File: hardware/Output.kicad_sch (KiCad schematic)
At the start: 26 parts, among them J10 Conn_Coaxial, J11 Conn_Coaxial, J12 Conn_Coaxial, J13 Conn_Coaxial, J14 Conn_Coaxial, J15 Conn_Coaxial, J8 Conn_Coaxial, J9 Conn_Coaxial, U29 74LVCH2T45DC, U30 74LVCH2T45DC

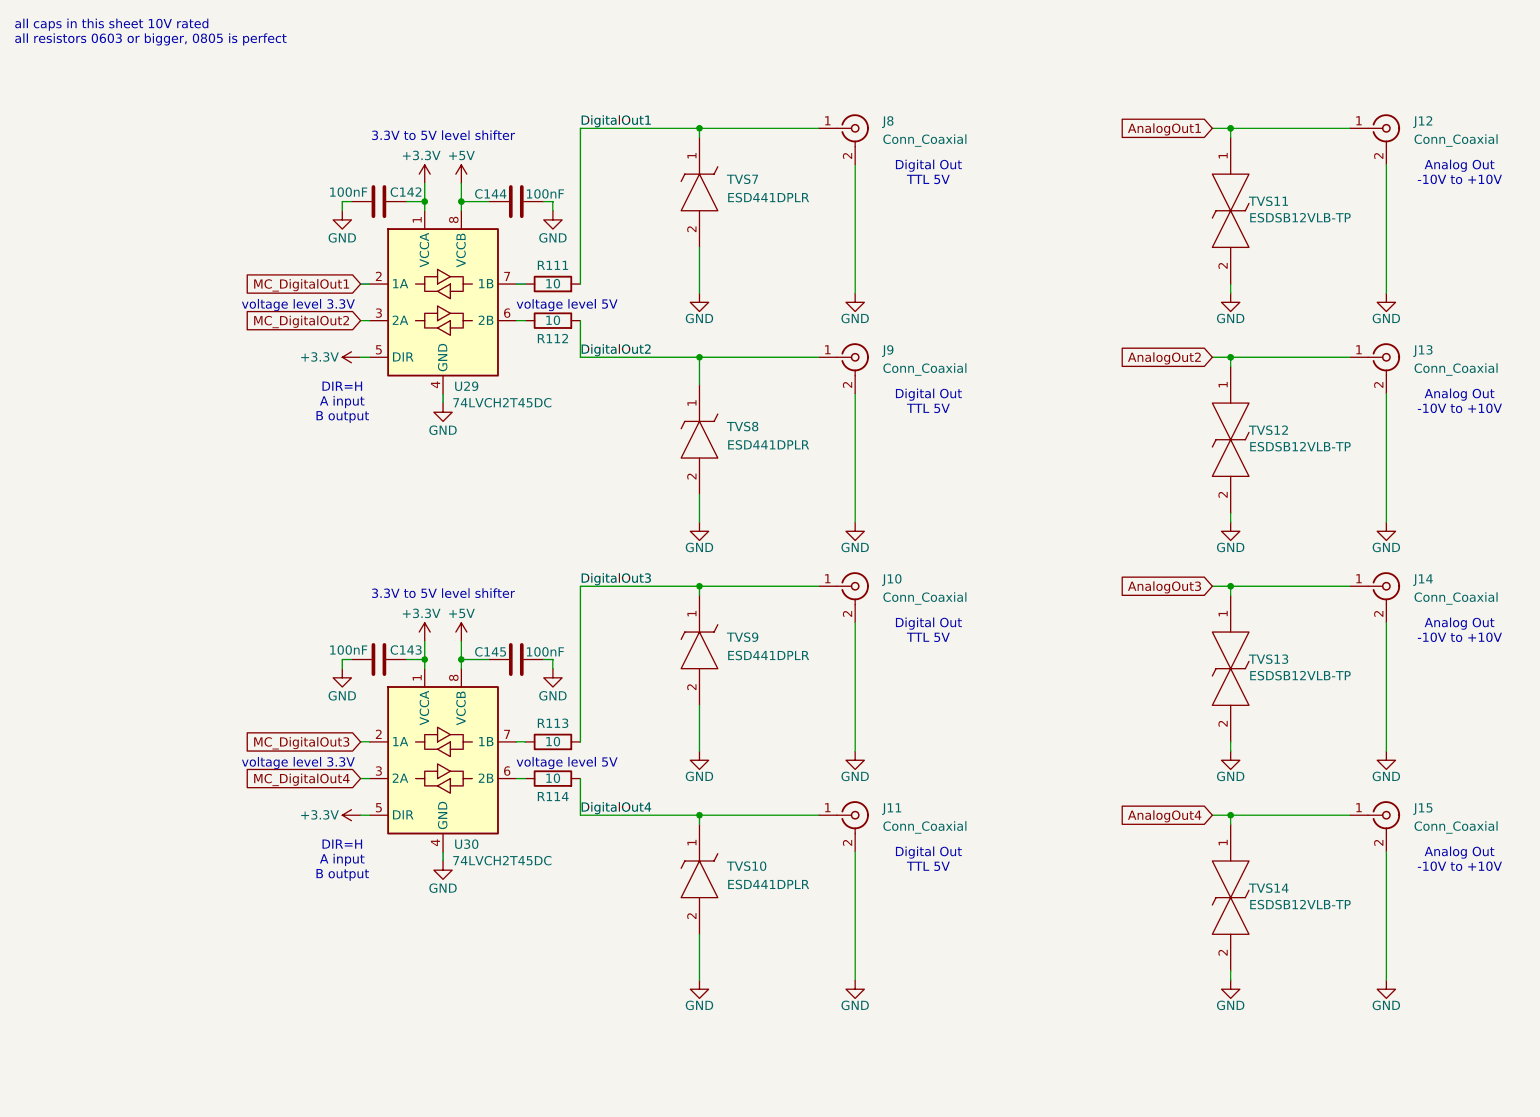
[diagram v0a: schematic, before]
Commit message: Added caps voltage rating + block diagram
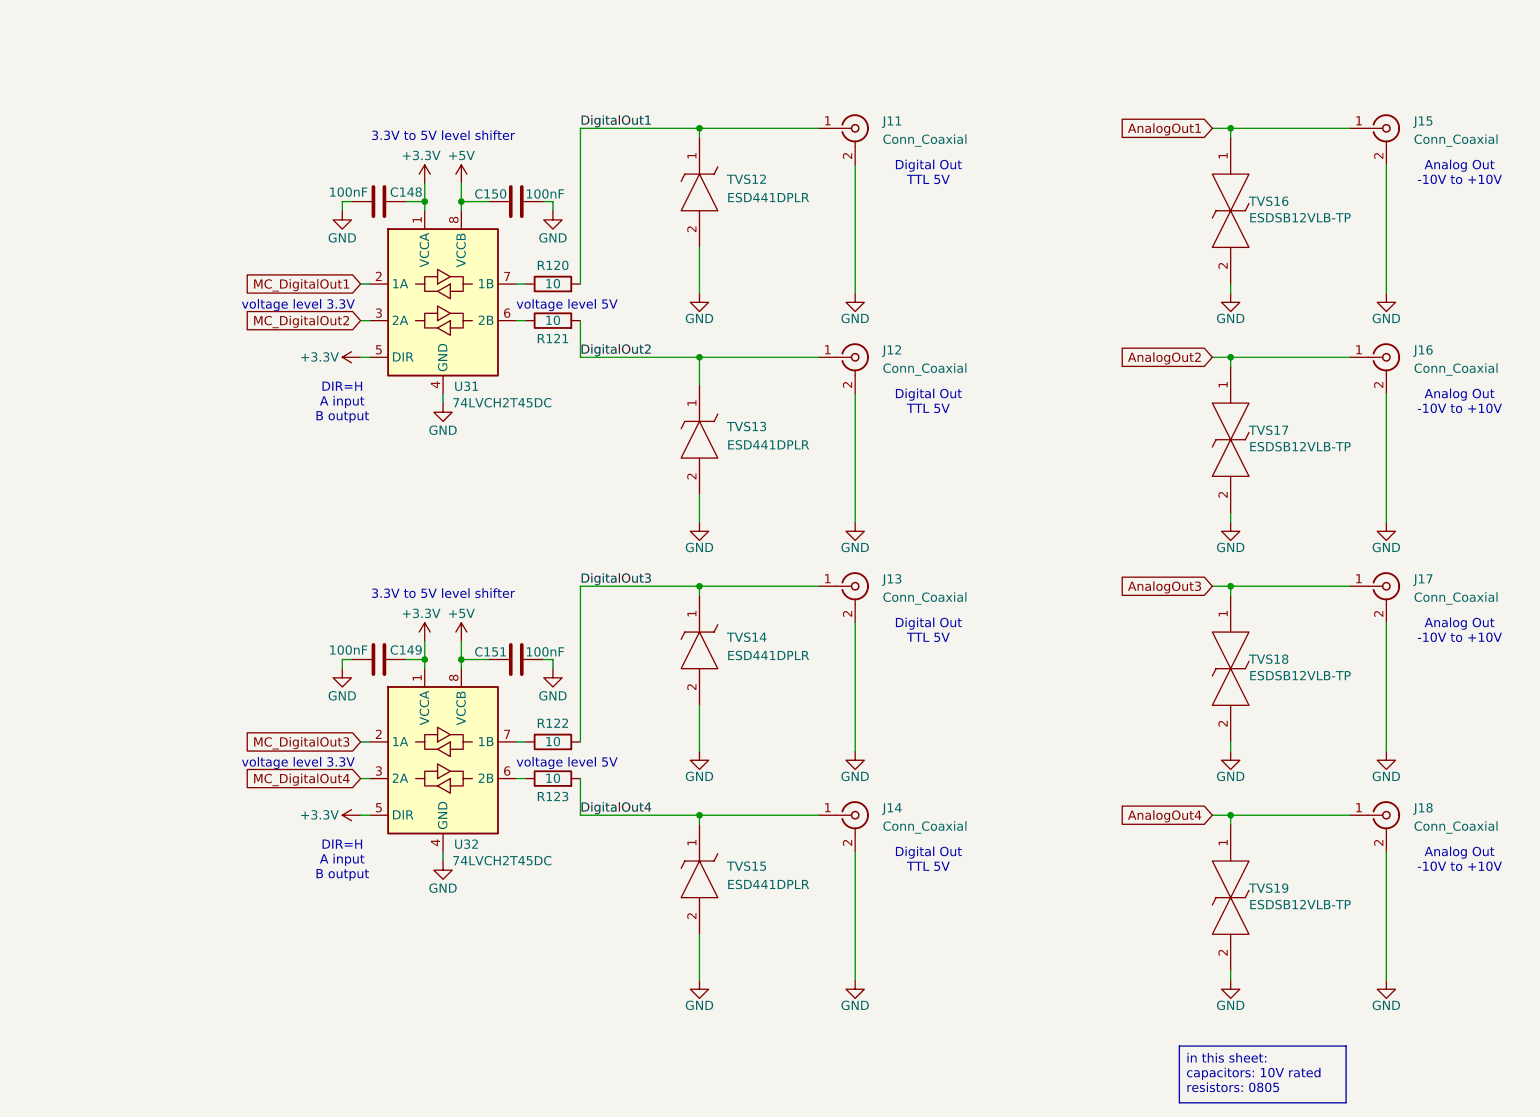
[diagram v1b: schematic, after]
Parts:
- renumbered C142 to C148, C143 to C149, C144 to C150, C145 to C151, J8 to J11, J9 to J12, J10 to J13, J11 to J14, J12 to J15, J13 to J16, J14 to J17, J15 to J18, R111 to R120, R112 to R121, R113 to R122, R114 to R123, TVS7 to TVS12, TVS8 to TVS13, TVS9 to TVS14, TVS10 to TVS15, TVS11 to TVS16, TVS12 to TVS17, TVS13 to TVS18, TVS14 to TVS19, U29 to U31, U30 to U32
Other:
- note removed: "all caps in this sheet 10V rated all resistors 0603 or bigger, 0805 is perfect"
- title: Multi Channel HARP DAC -> harp device quad dac

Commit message: The footprint assigning and reviewing have started.
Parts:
- C148, C149, C150, C151: symbol Device:C -> harp.device.quad.dac:C
- J11, J12, J13, J14, J15, J16, J17, J18: symbol Connector:Conn_Coaxial -> harp.device.quad.dac:Conn_Coaxial
- R120, R121, R122, R123: symbol Device:R -> harp.device.quad.dac:R
- TVS12, TVS13, TVS14, TVS15: symbol ESD441DPLR:ESD441DPLR -> harp.device.quad.dac:ESD441DPLR
- TVS16, TVS17, TVS18, TVS19: symbol ESDSB12VLB-TP:ESDSB12VLB-TP -> harp.device.quad.dac:ESDSB12VLB-TP
- U31, U32: symbol Logic_LevelTranslator:74LVCH2T45DC -> harp.device.quad.dac:74LVCH2T45DC
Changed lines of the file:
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@@
 	)
 	(symbol
-		(lib_id "Device:R")
+		(lib_id "harp.device.quad.dac:R")
 		(at 90.17 120.65 90)
 		(unit 1)
@@
 	)
 	(symbol
-		(lib_id "Connector:Conn_Coaxial")
+		(lib_id "harp.device.quad.dac:Conn_Coaxial")
 		(at 132.08 125.73 0)
 		(unit 1)
@@
 	)
 	(symbol
-		(lib_id "ESD441DPLR:ESD441DPLR")
+		(lib_id "harp.device.quad.dac:ESD441DPLR")
 		(at 110.49 95.25 270)
 		(unit 1)
@@
 	)
 	(symbol
-		(lib_id "Connector:Conn_Coaxial")
+		(lib_id "harp.device.quad.dac:Conn_Coaxial")
 		(at 205.74 62.23 0)
 		(unit 1)
@@
 	)
 	(symbol
-		(lib_id "Connector:Conn_Coaxial")
+		(lib_id "harp.device.quad.dac:Conn_Coaxial")
 		(at 205.74 125.73 0)
 		(unit 1)
@@
 	)
 	(symbol
-		(lib_id "Connector:Conn_Coaxial")
+		(lib_id "harp.device.quad.dac:Conn_Coaxial")
 		(at 132.08 62.23 0)
 		(unit 1)
@@
 	)
 	(symbol
-		(lib_id "Connector:Conn_Coaxial")
+		(lib_id "harp.device.quad.dac:Conn_Coaxial")
 		(at 132.08 93.98 0)
 		(unit 1)
@@
 	)
 	(symbol
-		(lib_id "Connector:Conn_Coaxial")
+		(lib_id "harp.device.quad.dac:Conn_Coaxial")
 		(at 205.74 93.98 0)
 		(unit 1)
@@
 	)
 	(symbol
-		(lib_id "ESD441DPLR:ESD441DPLR")
+		(lib_id "harp.device.quad.dac:ESD441DPLR")
 		(at 110.49 31.75 270)
 		(unit 1)
@@
 	)
 	(symbol
-		(lib_id "Device:C")
+		(lib_id "harp.device.quad.dac:C")
 		(at 85.09 40.64 270)
 		(unit 1)
@@
 	)
 	(symbol
-		(lib_id "Connector:Conn_Coaxial")
+		(lib_id "harp.device.quad.dac:Conn_Coaxial")
 		(at 132.08 30.48 0)
 		(unit 1)
@@
 	)
 	(symbol
-		(lib_id "Logic_LevelTranslator:74LVCH2T45DC")
+		(lib_id "harp.device.quad.dac:74LVCH2T45DC")
 		(at 74.93 118.11 0)
 		(unit 1)
@@
 	)
 	(symbol
-		(lib_id "Device:C")
+		(lib_id "harp.device.quad.dac:C")
 		(at 66.04 40.64 270)
 		(unit 1)
@@
 	)
 	(symbol
-		(lib_id "Logic_LevelTranslator:74LVCH2T45DC")
+		(lib_id "harp.device.quad.dac:74LVCH2T45DC")
 		(at 74.93 54.61 0)
 		(unit 1)
@@
 	)
 	(symbol
-		(lib_id "Connector:Conn_Coaxial")
+		(lib_id "harp.device.quad.dac:Conn_Coaxial")
 		(at 205.74 30.48 0)
 		(unit 1)
@@
 	)
 	(symbol
-		(lib_id "ESD441DPLR:ESD441DPLR")
+		(lib_id "harp.device.quad.dac:ESD441DPLR")
 		(at 110.49 127 270)
 		(unit 1)
@@
 	)
 	(symbol
-		(lib_id "ESDSB12VLB-TP:ESDSB12VLB-TP")
+		(lib_id "harp.device.quad.dac:ESDSB12VLB-TP")
 		(at 184.15 95.25 270)
 		(unit 1)
@@
 	)
 	(symbol
-		(lib_id "Device:R")
+		(lib_id "harp.device.quad.dac:R")
 		(at 90.17 115.57 90)
 		(unit 1)
@@
 	)
 	(symbol
-		(lib_id "ESDSB12VLB-TP:ESDSB12VLB-TP")
+		(lib_id "harp.device.quad.dac:ESDSB12VLB-TP")
 		(at 184.15 31.75 270)
 		(unit 1)
@@
 	)
 	(symbol
-		(lib_id "Device:C")
+		(lib_id "harp.device.quad.dac:C")
 		(at 66.04 104.14 270)
 		(unit 1)
@@
 	)
 	(symbol
-		(lib_id "Device:R")
+		(lib_id "harp.device.quad.dac:R")
 		(at 90.17 57.15 90)
 		(unit 1)
@@
 	)
 	(symbol
-		(lib_id "ESDSB12VLB-TP:ESDSB12VLB-TP")
+		(lib_id "harp.device.quad.dac:ESDSB12VLB-TP")
 		(at 184.15 127 270)
 		(unit 1)
@@
 	)
 	(symbol
-		(lib_id "Device:C")
+		(lib_id "harp.device.quad.dac:C")
 		(at 85.09 104.14 270)
 		(unit 1)
@@
 	)
 	(symbol
-		(lib_id "ESDSB12VLB-TP:ESDSB12VLB-TP")
+		(lib_id "harp.device.quad.dac:ESDSB12VLB-TP")
 		(at 184.15 63.5 270)
 		(unit 1)
@@
 	)
 	(symbol
-		(lib_id "Device:R")
+		(lib_id "harp.device.quad.dac:R")
 		(at 90.17 52.07 90)
 		(unit 1)
@@
 	)
 	(symbol
-		(lib_id "ESD441DPLR:ESD441DPLR")
+		(lib_id "harp.device.quad.dac:ESD441DPLR")
 		(at 110.49 66.04 270)
 		(unit 1)

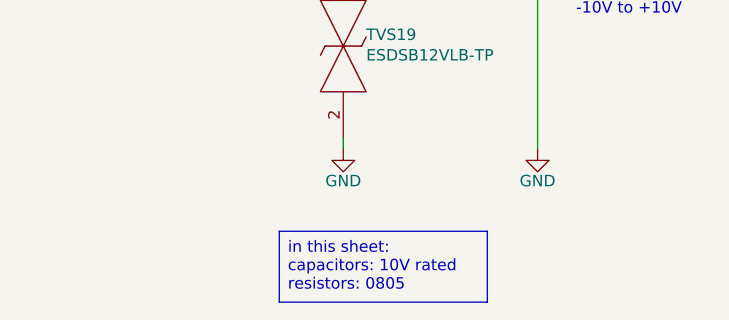
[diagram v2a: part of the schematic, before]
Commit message: Modified notes about caps and resistors
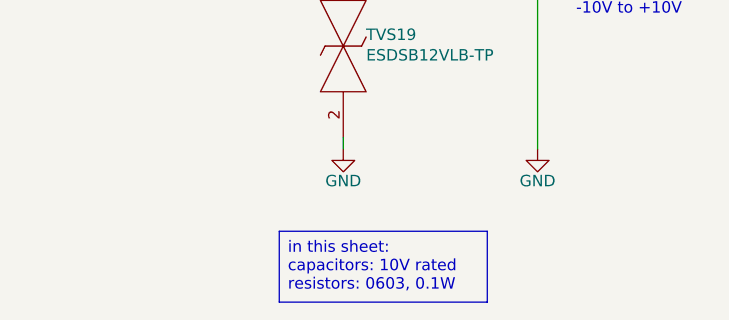
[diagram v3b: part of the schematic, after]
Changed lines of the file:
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@@
 		)
 	)
-	(text_box "in this sheet:\ncapacitors: 10V rated\nresistors: 0805"
+	(text_box "in this sheet:\ncapacitors: 10V rated\nresistors: 0603, 0.1W"
 		(exclude_from_sim no)
 		(at 177.038 157.734 0)

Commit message: Updating some footprints
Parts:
- C148, C149, C150, C151: footprint Capacitor_SMD:C_0402_1005Metric -> Capacitor_SMD:C_0603_1608Metric; symbol harp.device.quad.dac:C -> harp.device.quad.dac:C_0603
- R120, R121, R122, R123: footprint Resistor_SMD:R_0603_1608Metric_Pad0.98x0.95mm_HandSolder -> Resistor_SMD:R_0603_1608Metric; symbol harp.device.quad.dac:R -> harp.device.quad.dac:R_0603

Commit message: The layout design has begun.
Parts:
- J11, J12, J13, J14, J15, J16, J17, J18: footprint kicad_component_library:SMA_TE_Connectivity_CONSMA002-SMD-G-T_Horizontal -> harp.device.quad.dac.kicad:SMA_TE_Connectivity_CONSMA002-SMD-G-T_Horizontal
- TVS12, TVS13, TVS14, TVS15: footprint ESD441DPLR -> harp.device.quad.dac.kicad:ESD441DPLR
- U31, U32: footprint Package_SO:VSSOP-8_2.3x2mm_P0.5mm -> harp.device.quad.dac.kicad:VSSOP-8_2.3x2mm_P0.5mm
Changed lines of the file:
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@@
 			)
 		)
-		(property "Footprint" "kicad_component_library:SMA_TE_Connectivity_CONSMA002-SMD-G-T_Horizontal"
+		(property "Footprint" "harp.device.quad.dac.kicad:SMA_TE_Connectivity_CONSMA002-SMD-G-T_Horizontal"
 			(at 132.08 125.73 0)
 			(effects
@@
 			)
 		)
-		(property "Footprint" "ESD441DPLR"
+		(property "Footprint" "harp.device.quad.dac.kicad:ESD441DPLR"
 			(at 114.3 105.41 0)
 			(effects
@@
 			)
 		)
-		(property "Footprint" "kicad_component_library:SMA_TE_Connectivity_CONSMA002-SMD-G-T_Horizontal"
+		(property "Footprint" "harp.device.quad.dac.kicad:SMA_TE_Connectivity_CONSMA002-SMD-G-T_Horizontal"
 			(at 205.74 62.23 0)
 			(effects
@@
 			)
 		)
-		(property "Footprint" "kicad_component_library:SMA_TE_Connectivity_CONSMA002-SMD-G-T_Horizontal"
+		(property "Footprint" "harp.device.quad.dac.kicad:SMA_TE_Connectivity_CONSMA002-SMD-G-T_Horizontal"
 			(at 205.74 125.73 0)
 			(effects
@@
 			)
 		)
-		(property "Footprint" "kicad_component_library:SMA_TE_Connectivity_CONSMA002-SMD-G-T_Horizontal"
+		(property "Footprint" "harp.device.quad.dac.kicad:SMA_TE_Connectivity_CONSMA002-SMD-G-T_Horizontal"
 			(at 132.08 62.23 0)
 			(effects
@@
 			)
 		)
-		(property "Footprint" "kicad_component_library:SMA_TE_Connectivity_CONSMA002-SMD-G-T_Horizontal"
+		(property "Footprint" "harp.device.quad.dac.kicad:SMA_TE_Connectivity_CONSMA002-SMD-G-T_Horizontal"
 			(at 132.08 93.98 0)
 			(effects
@@
 			)
 		)
-		(property "Footprint" "kicad_component_library:SMA_TE_Connectivity_CONSMA002-SMD-G-T_Horizontal"
+		(property "Footprint" "harp.device.quad.dac.kicad:SMA_TE_Connectivity_CONSMA002-SMD-G-T_Horizontal"
 			(at 205.74 93.98 0)
 			(effects
@@
 			)
 		)
-		(property "Footprint" "ESD441DPLR"
+		(property "Footprint" "harp.device.quad.dac.kicad:ESD441DPLR"
 			(at 114.3 41.91 0)
 			(effects
@@
 			)
 		)
-		(property "Footprint" "kicad_component_library:SMA_TE_Connectivity_CONSMA002-SMD-G-T_Horizontal"
+		(property "Footprint" "harp.device.quad.dac.kicad:SMA_TE_Connectivity_CONSMA002-SMD-G-T_Horizontal"
 			(at 132.08 30.48 0)
 			(effects
@@
 			)
 		)
-		(property "Footprint" "Package_SO:VSSOP-8_2.3x2mm_P0.5mm"
+		(property "Footprint" "harp.device.quad.dac.kicad:VSSOP-8_2.3x2mm_P0.5mm"
 			(at 74.93 139.7 0)
 			(effects
@@
 			)
 		)
-		(property "Footprint" "Package_SO:VSSOP-8_2.3x2mm_P0.5mm"
+		(property "Footprint" "harp.device.quad.dac.kicad:VSSOP-8_2.3x2mm_P0.5mm"
 			(at 74.93 76.2 0)
 			(effects
@@
 			)
 		)
-		(property "Footprint" "kicad_component_library:SMA_TE_Connectivity_CONSMA002-SMD-G-T_Horizontal"
+		(property "Footprint" "harp.device.quad.dac.kicad:SMA_TE_Connectivity_CONSMA002-SMD-G-T_Horizontal"
 			(at 205.74 30.48 0)
 			(effects
@@
 			)
 		)
-		(property "Footprint" "ESD441DPLR"
+		(property "Footprint" "harp.device.quad.dac.kicad:ESD441DPLR"
 			(at 114.3 137.16 0)
 			(effects
@@
 			)
 		)
-		(property "Footprint" "ESD441DPLR"
+		(property "Footprint" "harp.device.quad.dac.kicad:ESD441DPLR"
 			(at 114.3 76.2 0)
 			(effects

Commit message: Some improvements have been made to the layout.
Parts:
- TVS16, TVS17, TVS18, TVS19: footprint ESDSB12VLBTP -> harp.device.quad.dac.kicad:ESDSB12VLBTP
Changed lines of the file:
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@@
 			)
 		)
-		(property "Footprint" "ESDSB12VLBTP"
+		(property "Footprint" "harp.device.quad.dac.kicad:ESDSB12VLBTP"
 			(at 187.96 107.95 0)
 			(effects
@@
 			)
 		)
-		(property "Footprint" "ESDSB12VLBTP"
+		(property "Footprint" "harp.device.quad.dac.kicad:ESDSB12VLBTP"
 			(at 187.96 44.45 0)
 			(effects
@@
 			)
 		)
-		(property "Footprint" "ESDSB12VLBTP"
+		(property "Footprint" "harp.device.quad.dac.kicad:ESDSB12VLBTP"
 			(at 187.96 139.7 0)
 			(effects
@@
 			)
 		)
-		(property "Footprint" "ESDSB12VLBTP"
+		(property "Footprint" "harp.device.quad.dac.kicad:ESDSB12VLBTP"
 			(at 187.96 76.2 0)
 			(effects

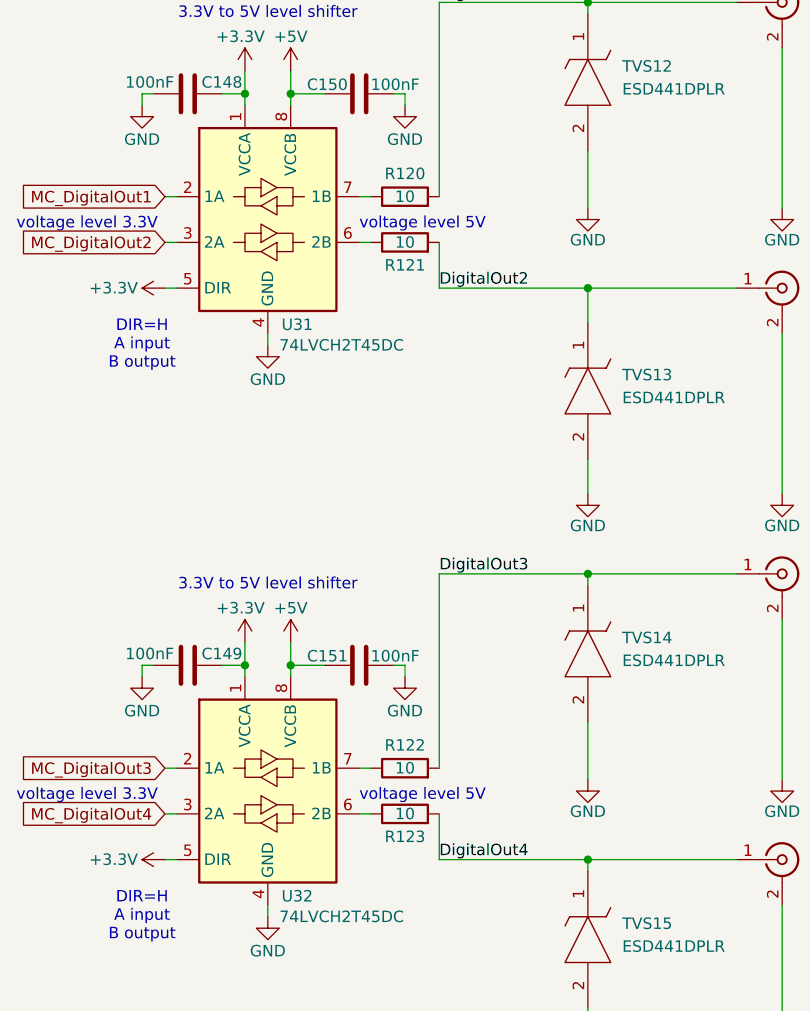
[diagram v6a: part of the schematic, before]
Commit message: The part designators have been reannotated.
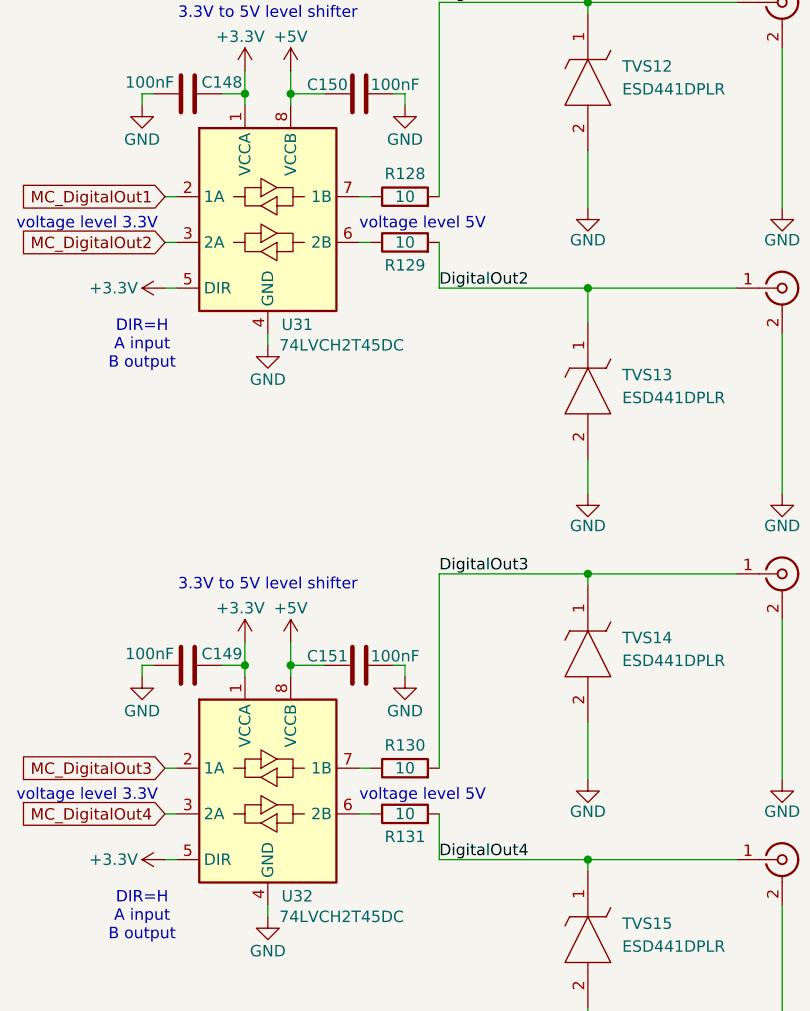
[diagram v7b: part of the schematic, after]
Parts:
- renumbered R120 to R128, R121 to R129, R122 to R130, R123 to R131
